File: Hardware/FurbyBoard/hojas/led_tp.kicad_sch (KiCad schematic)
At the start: 9 parts, among them J11 J_EXP: header de expansión 2 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

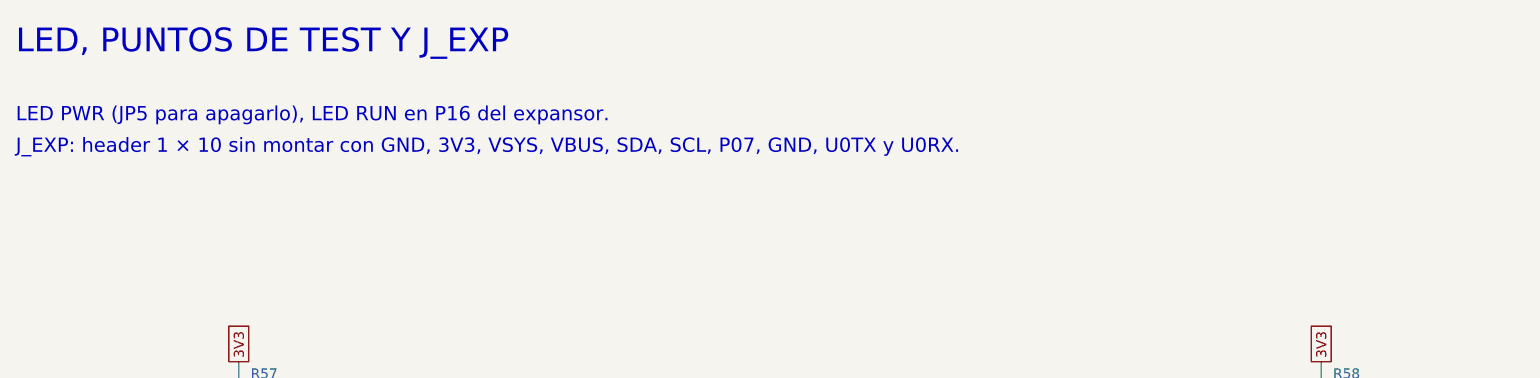
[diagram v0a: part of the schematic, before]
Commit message: Docs: notas del esquema y descripción de D5 al día con el mapa de pines final
Las notas de las hojas seguían con pines de antes del replanteo: JP1 libera
GPIO9 (no GPIO48), la INT del TCA9535 va a GPIO6 (no GPIO21), JP4 libera GPIO8
(no GPIO14) y el LED del encoder va desde V6 por 470 Ω (sin AO3400A); LED RUN en
P03 (no P16) y J_EXP 2 × 5 con el orden del bloque U. Sin cambios de redes.

Puertas: ERC 0, DRC con paridad 0/0 y 0 sin unir; cobre y rellenos idénticos.

Co-Authored-By: Claude Opus 5.5 (1M context) <noreply@anthropic.com>
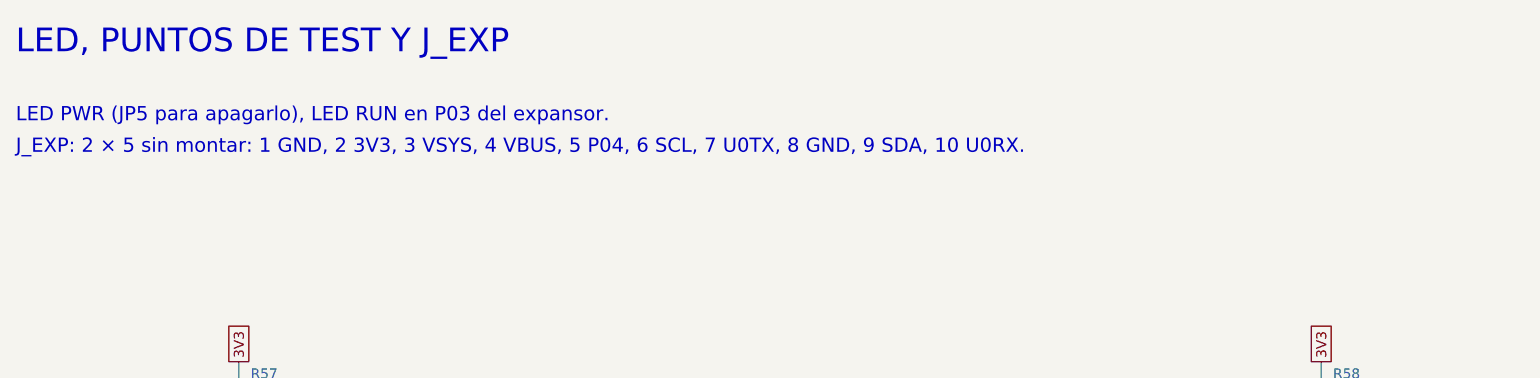
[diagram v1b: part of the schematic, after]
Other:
- note added: "J_EXP: 2 × 5 sin montar: 1 GND, 2 3V3, 3 VSYS, 4 VBUS, 5 P04, 6 SCL, 7 U0TX, 8 GND, 9 SDA, 10 U0RX."
- note added: "LED PWR (JP5 para apagarlo), LED RUN en P03 del expansor."
- note removed: "J_EXP: header 1 × 10 sin montar con GND, 3V3, VSYS, VBUS, SDA, SCL, P07, GND, U0TX y U0RX."
- note removed: "LED PWR (JP5 para apagarlo), LED RUN en P16 del expansor."
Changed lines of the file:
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@@
 		(comment 1 "Generado por scripts/gen_sch.py desde scripts/design.py: no editar a mano")
 	)
-	(text "J_EXP: header 1 × 10 sin montar con GND, 3V3, VSYS, VBUS, SDA, SCL, P07, GND, U0TX y U0RX."
+	(text "J_EXP: 2 × 5 sin montar: 1 GND, 2 3V3, 3 VSYS, 4 VBUS, 5 P04, 6 SCL, 7 U0TX, 8 GND, 9 SDA, 10 U0RX."
 		(exclude_from_sim no)
 		(at 20 34 0)
@@
 		)
 	)
-	(text "LED PWR (JP5 para apagarlo), LED RUN en P16 del expansor."
+	(text "LED PWR (JP5 para apagarlo), LED RUN en P03 del expansor."
 		(exclude_from_sim no)
 		(at 20 30 0)
@@
 			)
 		)
-		(property "Description" "LED RUN: latido del firmware (P16 del expansor)"
+		(property "Description" "LED RUN: latido del firmware (P03 del expansor)"
 			(at 228.6 66.04 0)
 			(hide yes)
